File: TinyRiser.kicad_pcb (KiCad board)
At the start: 4 copper layers, 113.2 x 23.5 mm, 27 parts, among them J2 Bus_PCI_Express_x16, J3 Bus_M.2_Socket_M

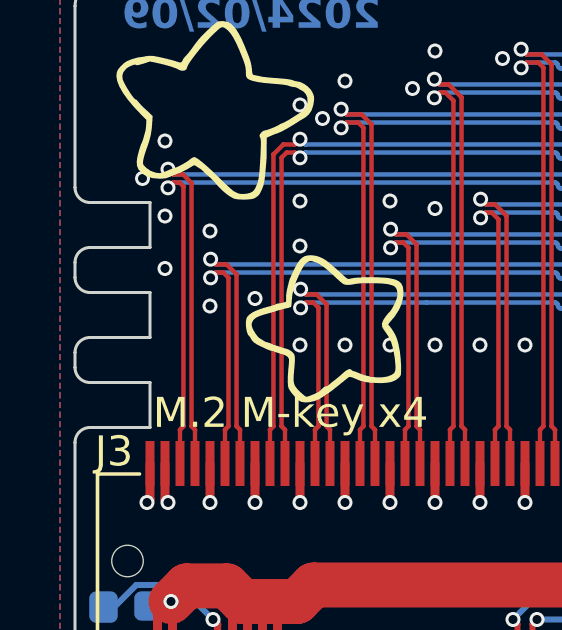
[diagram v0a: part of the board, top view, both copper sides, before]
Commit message: Upgraded to Kicad 8, Changed compatibility text, changed mount bracket slots, updated readme
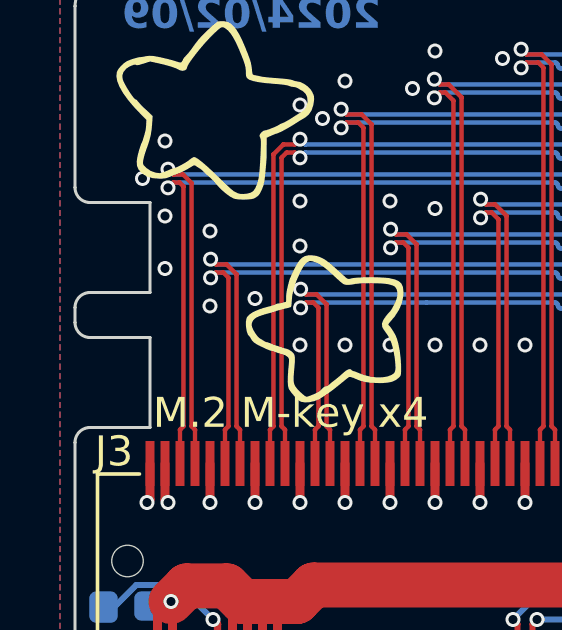
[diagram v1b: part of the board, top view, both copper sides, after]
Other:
- outline, holes or cut-outs redrawn
- board text added: "Compatible with Tiny5: Lenovo ThinkCentre M720q, M920q, M920x Tiny Lenovo ThinkStation P330 Tiny NEC Mate MC-3, MC-4, MC-5"
- board text removed: "Compatible with: Lenovo ThinkCentre M720q, M920q, M920x Tiny Lenovo ThinkStation P330 Tiny NEC Mate MC-3, MC-4, MC-5"

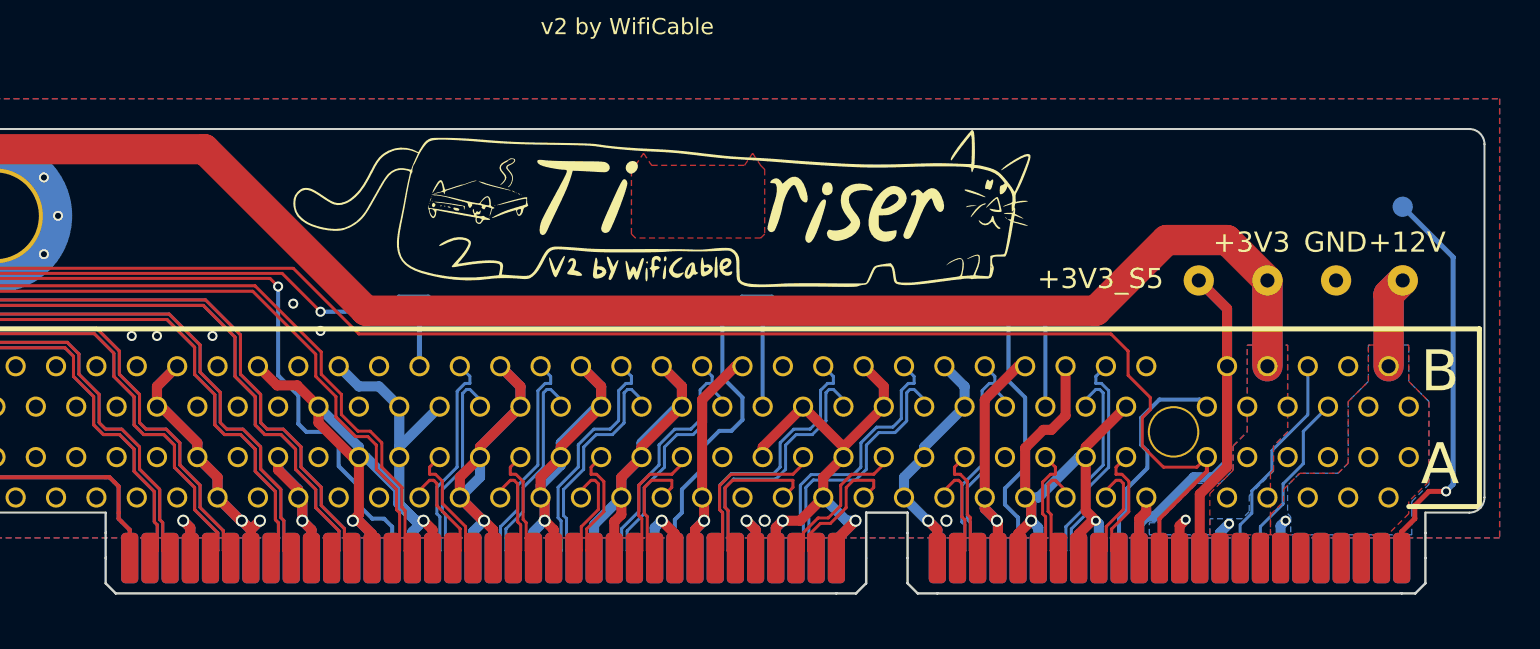
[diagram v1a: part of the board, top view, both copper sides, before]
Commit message: Adding fan header (unfinished)
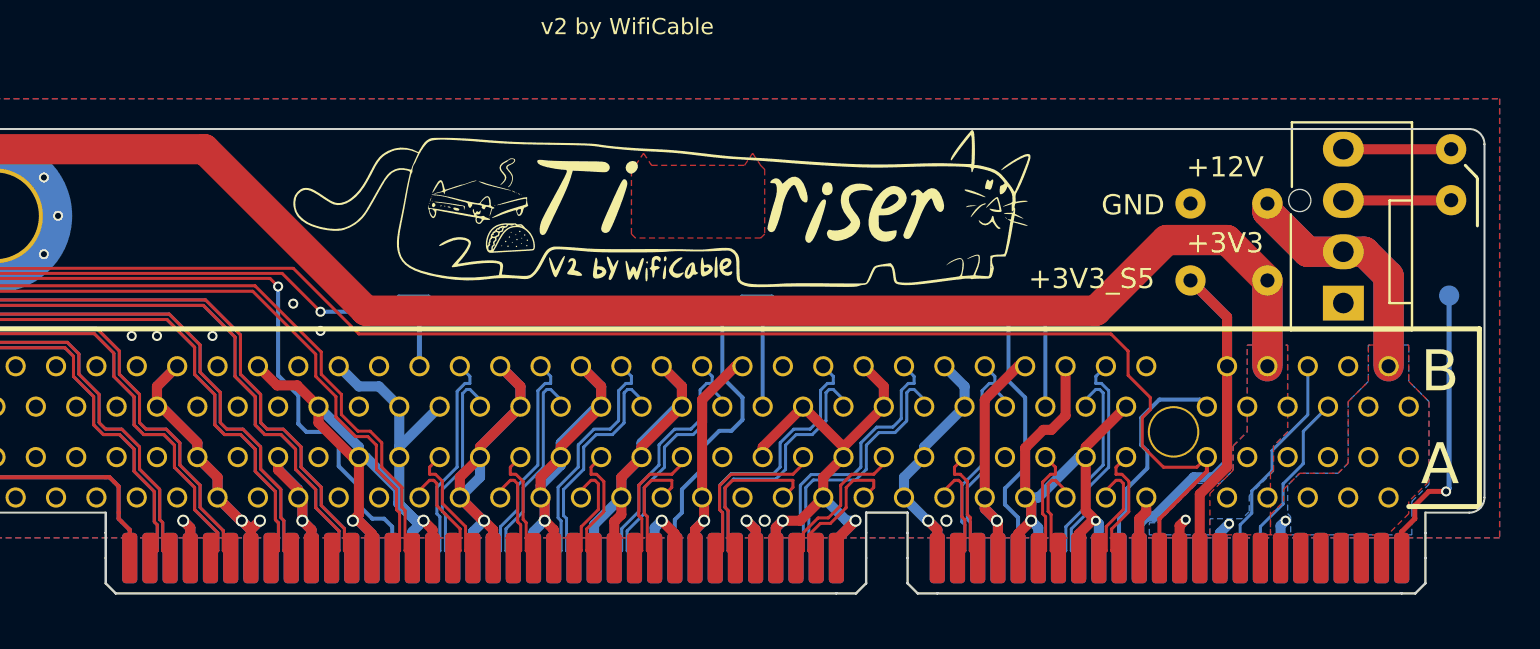
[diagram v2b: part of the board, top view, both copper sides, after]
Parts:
- added G***: LOGO, LOGO, F.Cu at (104.0, 124.9)
- added M1: Fan_4pin, Connector:FanPinHeader_1x04_P2.54mm_Vertical, F.Cu at (145.3, 128.1)
- added TP10: Taco, TestPoint:TestPoint_THTPad_D1.5mm_Drill0.7mm, F.Cu at (150.6, 123.0)
- added TP11: PWM, TestPoint:TestPoint_THTPad_D1.5mm_Drill0.7mm, F.Cu at (150.6, 120.5)
- moved TP6 8.15 mm to (137.7, 123.2)
- moved TP9 7.71 mm to (141.5, 123.2)
- moved TP1 4.96 mm to (150.5, 127.8)
- moved TP5 0.41 mm to (137.7, 127.0)
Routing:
- net +12V: track 9.08 -> 24.4 mm
- net Net-(J1-PCIE_SOLT_A60): track 20.0 -> 14.5 mm
- net Net-(M1-Tacho): track 0.00 -> 5.35 mm
- net Net-(M1-PWM): track 0.00 -> 5.34 mm

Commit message: Mostly finished fan connector implementation
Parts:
- removed TP10: Taco, TestPoint:TestPoint_THTPad_D1.5mm_Drill0.7mm
- removed TP11: PWM, TestPoint:TestPoint_THTPad_D1.5mm_Drill0.7mm
- added J4: fancontrol_header, Connector_PinSocket_2.54mm:PinSocket_2x03_P2.54mm_Horizontal, F.Cu at (148.3, 126.7)
- added R6: 0R, Resistor_SMD:R_0603_1608Metric_Pad0.98x0.95mm_HandSolder, F.Cu at (1.68, 0.76)
- moved M1 7.85 mm to (143.3, 120.5), turned to -90 degrees
- moved TP4 4.20 mm to (137.3, 127.1)
- moved TP5 4.20 mm to (133.5, 127.1)
- moved TP6 4.20 mm to (133.5, 123.2)
- moved TP9 4.20 mm to (137.3, 123.2)
- moved TP1 4.15 mm to (150.5, 131.9)
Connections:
- M1 pad 2: +12V -> +12V_fan
- M1 pad 3: Net-(M1-Tacho) -> Taco_fan
- M1 pad 4: Net-(M1-PWM) -> PWM_fan
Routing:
- net +3V3: track 151.0 -> 157.3 mm
- net PWM_fan: track 0.00 -> 5.58 mm
- net Taco_fan: track 0.00 -> 5.58 mm
- net +12V_fan: track 0.00 -> 5.58 mm
- net Net-(M1-Tacho): track 5.35 -> 0.00 mm
- net Net-(M1-PWM): track 5.34 -> 0.00 mm
- net Net-(J1-PCIE_SOLT_A60): track 14.5 -> 10.3 mm
- net +3V3_S5: track 32.2 -> 29.9 mm
- net +12V: track 24.4 -> 26.2 mm

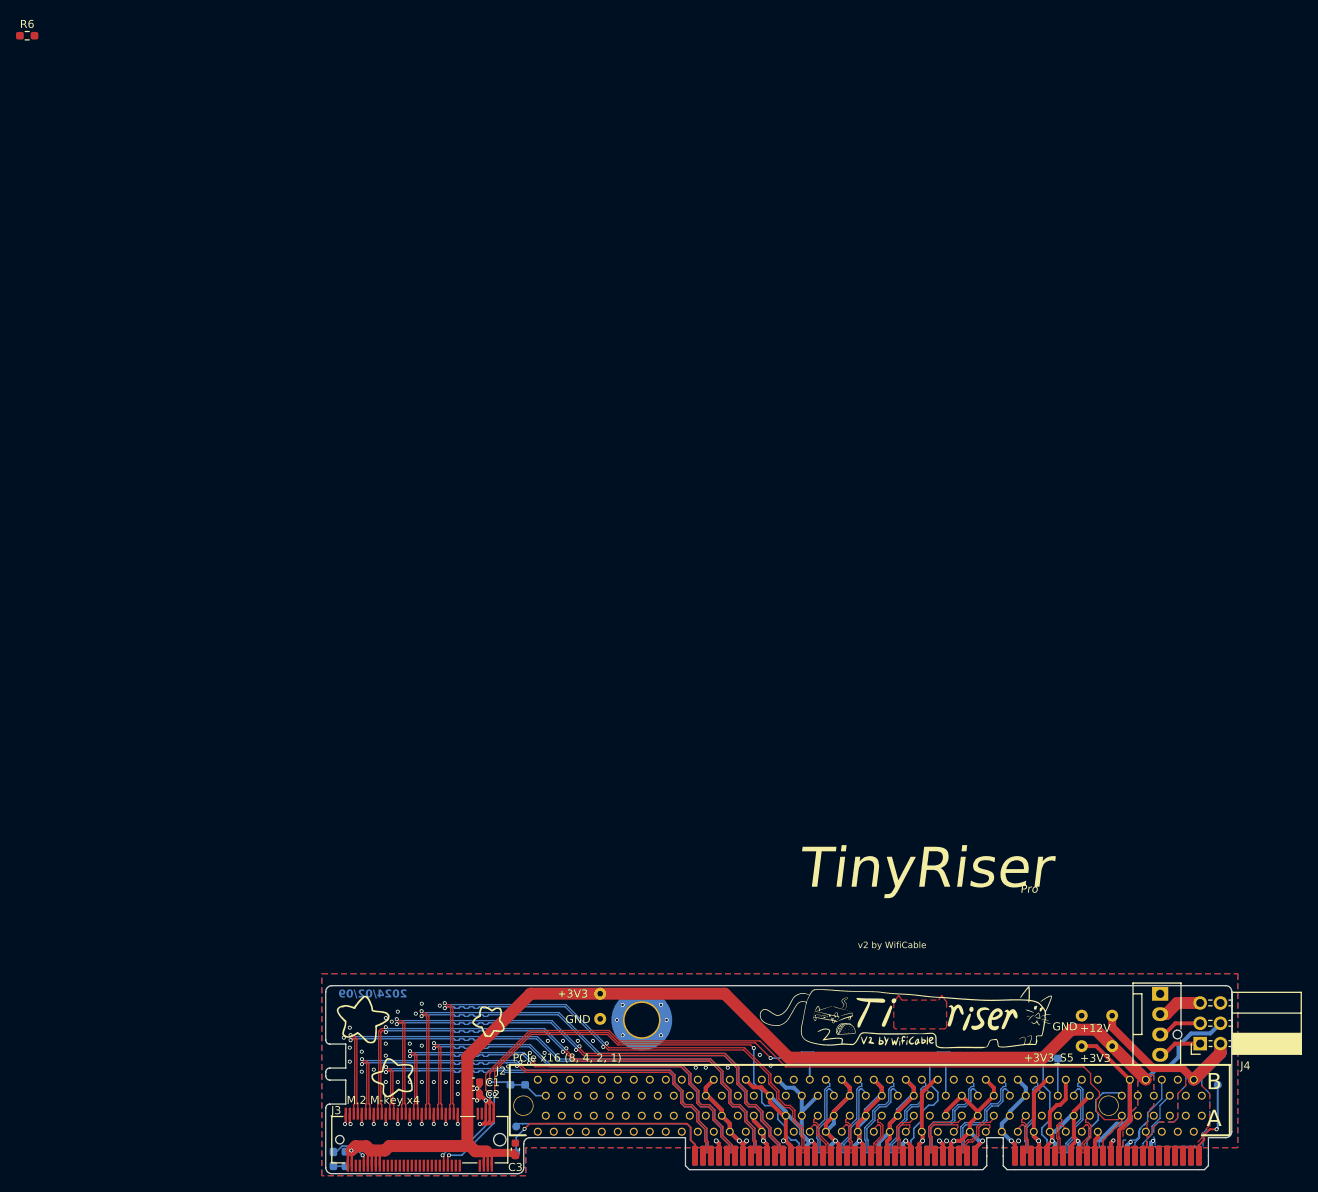
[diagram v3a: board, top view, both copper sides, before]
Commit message: swapped fan header for right angle pin header
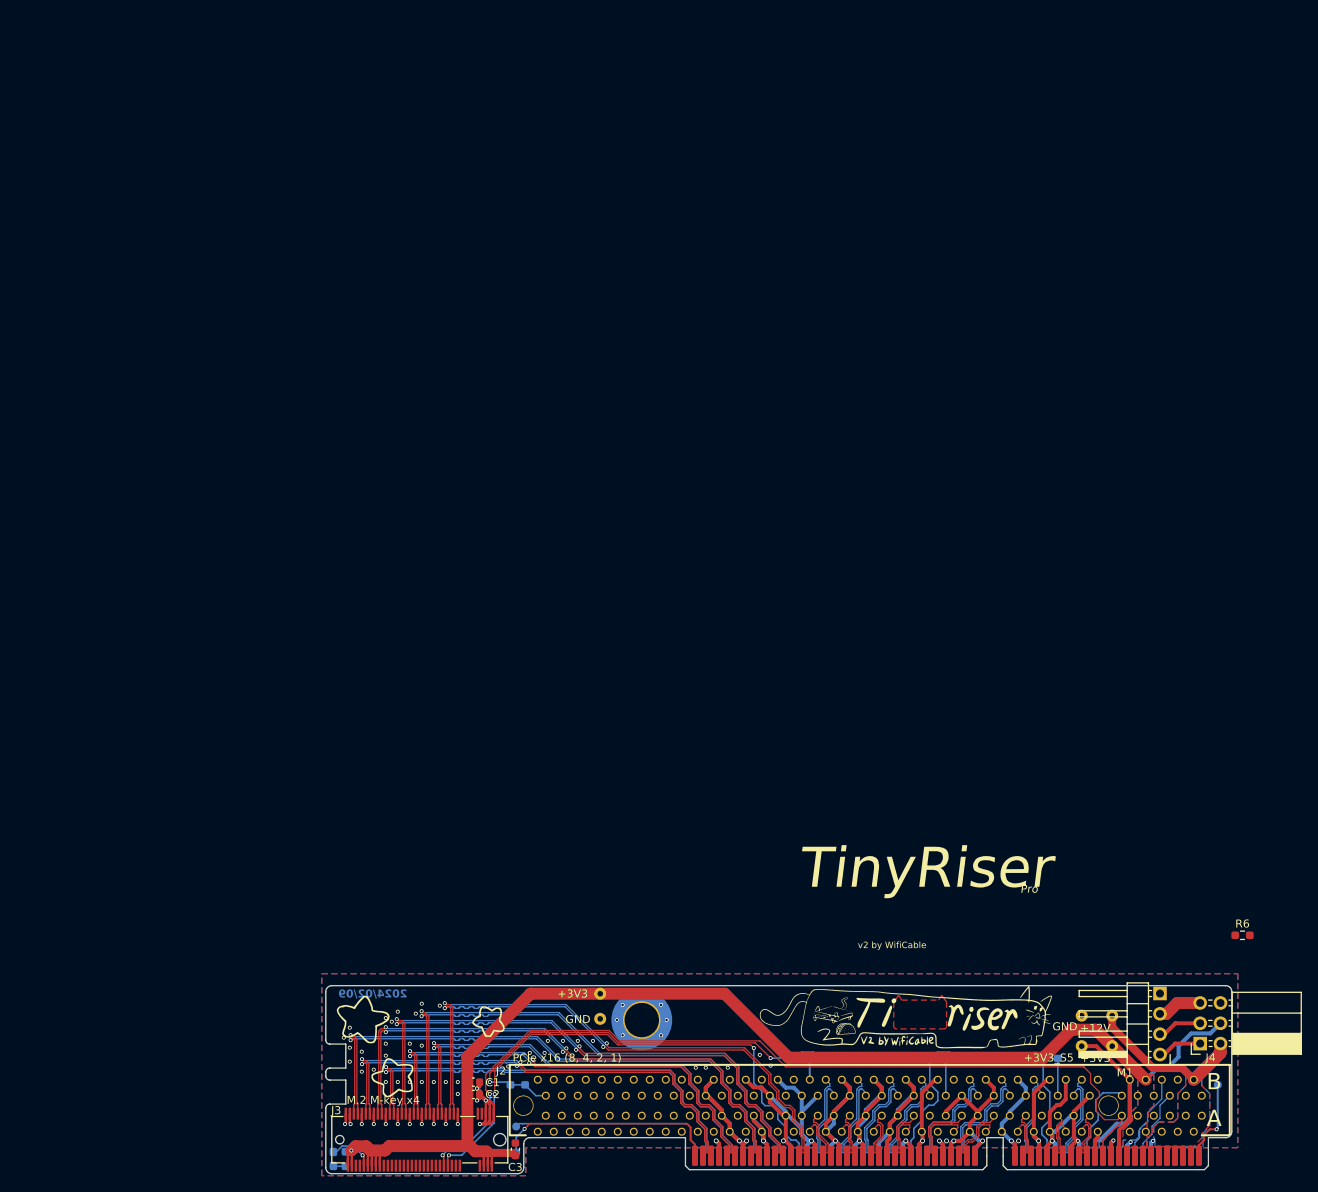
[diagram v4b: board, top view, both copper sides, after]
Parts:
- M1: footprint Connector:FanPinHeader_1x04_P2.54mm_Vertical -> Connector_PinHeader_2.54mm:PinHeader_1x04_P2.54mm_Horizontal
- moved R6 189.0 mm to (153.6, 113.2)
- moved M1 7.58 mm to (143.3, 128.1), turned to 180 degrees
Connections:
- R6 pad 1: unconnected-(R6-Pad1) -> +12V_fan
- R6 pad 2: unconnected-(R6-Pad2) -> +12V

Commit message: Finished fan header implementation
Somehow it doesn't feel like it's done but it is???
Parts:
- added G***: LOGO, LOGO, B.Cu at (140.0, 124.2)
- G***: moved to B.Cu
- R2: renamed from R6; footprint Resistor_SMD:R_0603_1608Metric_Pad0.98x0.95mm_HandSolder -> Resistor_SMD:R_0805_2012Metric_Pad1.20x1.40mm_HandSolder; moved to B.Cu
- moved G*** 36.5 mm to (139.0, 114.7), turned to 180 degrees
- moved R2 15.9 mm to (149.3, 128.5)
- moved M1 1.63 mm to (144.9, 128.2)
- renumbered R2 to R3, R3 to R4, R4 to R5, R5 to R6
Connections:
- J4 pad 1: PWM_fan -> +12V_fan
- J4 pad 5: +12V_fan -> PWM_fan
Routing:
- net PWM_fan: track 5.59 -> 3.86 mm
- net Taco_fan: track 5.59 -> 3.86 mm
- net +3V3: track 157.3 -> 158.5 mm
- net +12V: track 26.2 -> 26.9 mm
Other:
- board text added: "12V"
- board text added: "12V FAN"
- board text added: "3V3"
- board text added: "PWM"
- board text added: "notch"

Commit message: updated pcb datecode lol
why do i even put that on there
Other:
- board text added: "2024/05/15"
- board text removed: "2024/02/09"
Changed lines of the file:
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@@
 		(layer "User.2")
 	)
-	(gr_text "2024/02/09"
+	(gr_text "2024/05/15"
 		(at 49.2 121.1 0)
 		(layer "B.Cu")
